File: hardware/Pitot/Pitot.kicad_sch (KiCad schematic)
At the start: 35 parts, among them J1 53307-2471, J2 Conn_01x05, J3 MX150_02x06_Vertical, U2 LDO40LPURY

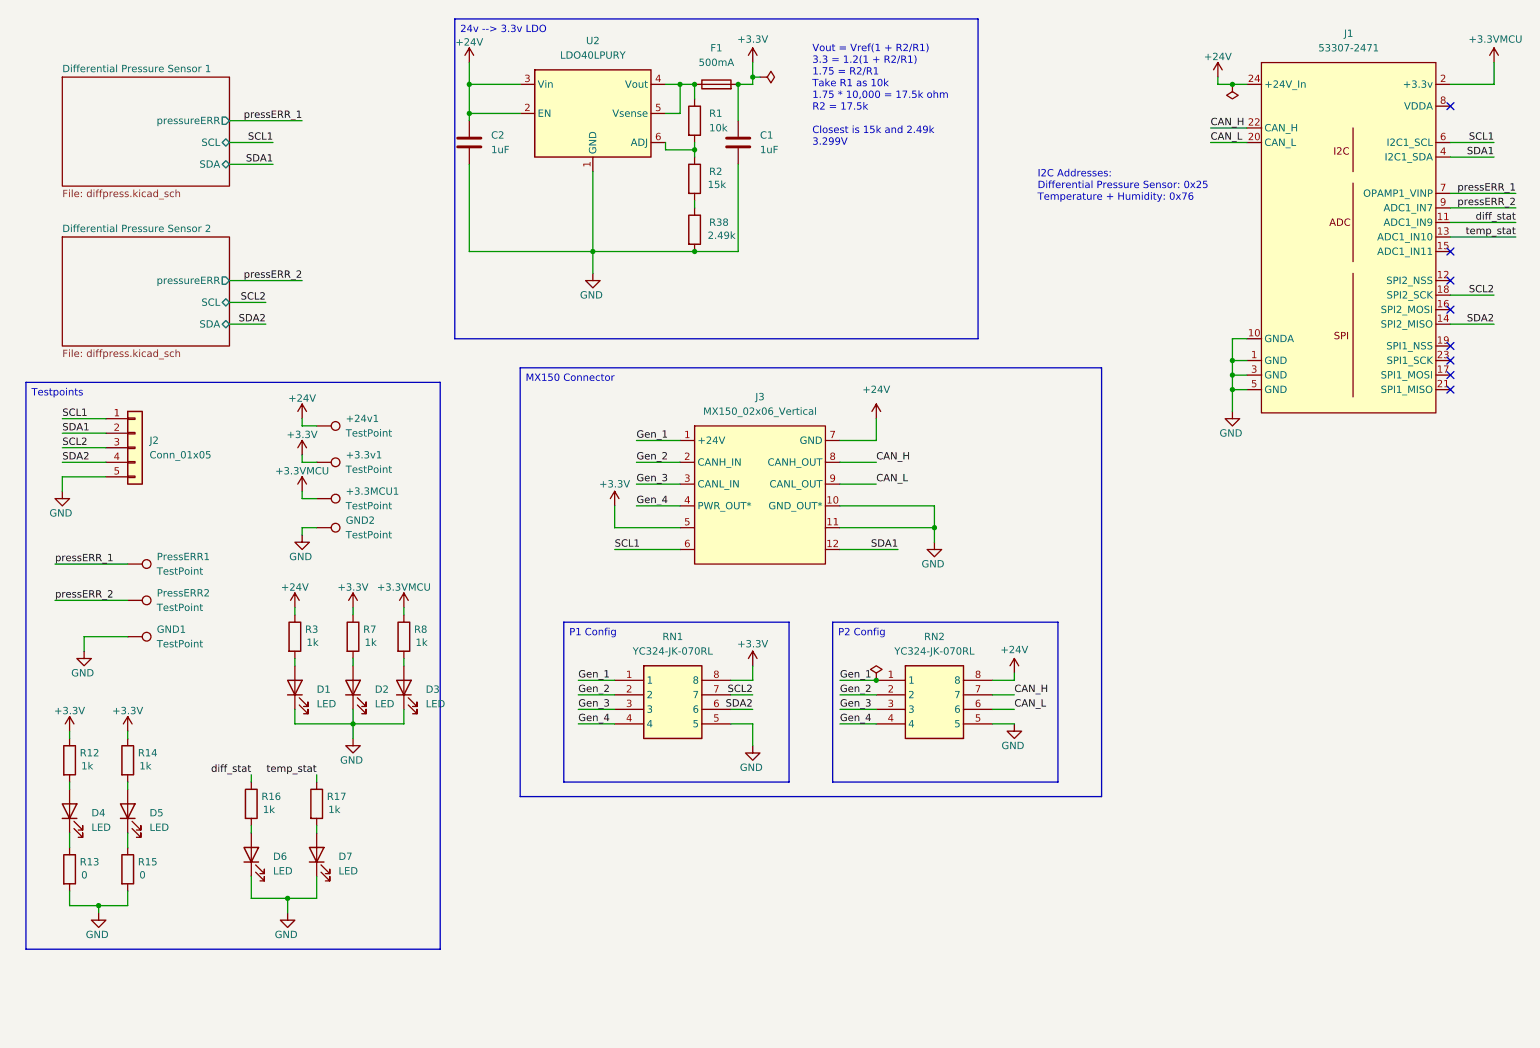
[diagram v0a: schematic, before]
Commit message: small changes, cubemx needs checking
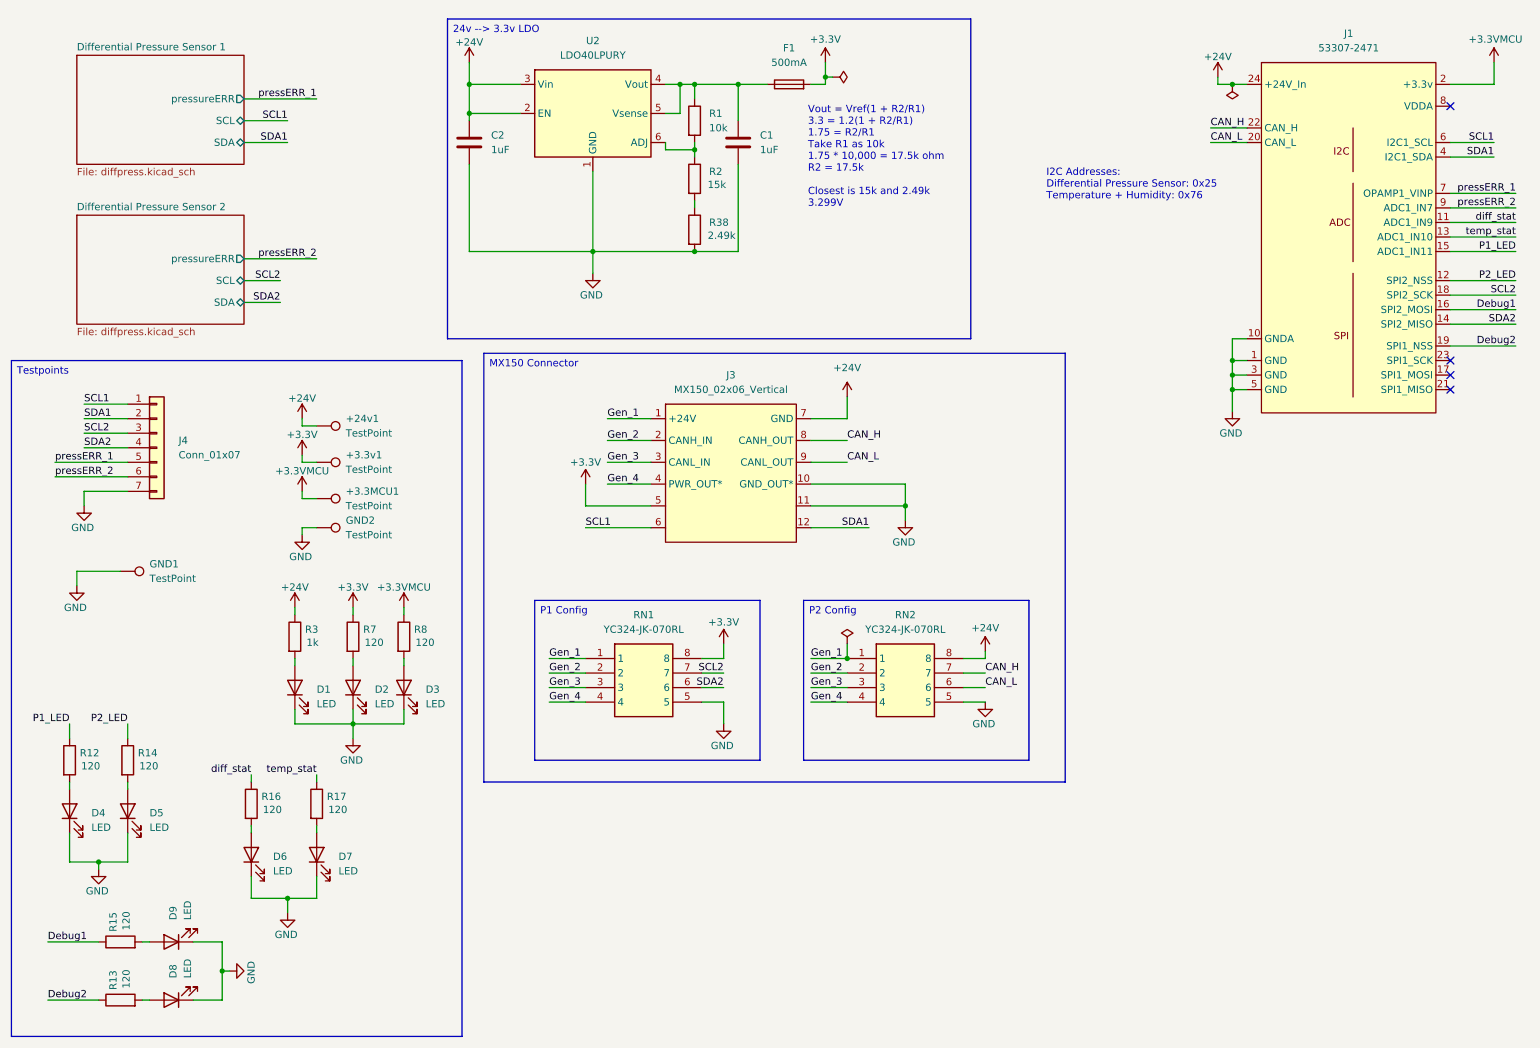
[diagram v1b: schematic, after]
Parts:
- removed J2: Conn_01x05, Connector_PinSocket_2.54mm:PinSocket_1x05_P2.54mm_Vertical, symbol Connector_Generic:Conn_01x05
- removed PressERR1, PressERR2: TestPoint, TestPoint:TestPoint_Pad_1.0x1.0mm, symbol Connector:TestPoint
- added D8, D9: LED, LED_SMD:LED_0603_1608Metric_Pad1.05x0.95mm_HandSolder, symbol Device:LED
- added J4: Conn_01x07, symbol Connector_Generic:Conn_01x07
- R12, R14, R16, R17, R7, R8: value 1k -> 120
- R13, R15: value 0 -> 120; P/N CRCW06030000Z0EE -> CRCW06031K00FKEI
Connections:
- net +3.3V: no longer C1.1, R12.1, R14.1
- net GND: now also D4.1 (K), D5.1 (K), D8.1 (K), D9.1 (K), J4.7 (Pin_7); no longer R13.2, R15.2
- net SCL1: now also J4.1 (Pin_1)
- net SCL2: now also J4.3 (Pin_3)
- net SDA1: now also J4.2 (Pin_2)
- net SDA2: now also J4.4 (Pin_4)
- net pressERR_1: now also J4.5 (Pin_5)
- net pressERR_2: now also J4.6 (Pin_6)
- net Debug2: now reaches R13.1
- net Debug2: now also J1.19 (SPI1_NSS); no longer D4.1 (K)
- net at F1.1, R1.1, U2.4 (Vout)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: now also C1.1
- net P2_LED: now reaches J1.12 (SPI2_NSS)
- net P2_LED: now also R14.1
- net P1_LED: now reaches J1.15 (ADC1_IN11)
- net P1_LED: now also R12.1
- net Debug1: now reaches J1.16 (SPI2_MOSI)
- net Debug1: now also R15.1
- new net: D9.2 (A), R15.2
- new net: D8.2 (A), R13.2
- no-connect marks 8 -> 4
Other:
- moved on the sheet: F1, GND1, J3, RN1, RN2

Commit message: finished layout
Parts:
- J4: footprint (none) -> Connector_PinHeader_2.54mm:PinHeader_2x04_P2.54mm_Vertical
- R3: value 1k -> 4.7k
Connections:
- net +24V: now also RN2.5; no longer RN2.8
- net GND: now also RN2.8; no longer RN2.5
- net Gen_1: now also RN2.4; no longer RN2.1
- net Gen_2: now also RN1.3; no longer RN1.2
- net Gen_3: now also RN1.2; no longer RN1.3
- net Gen_4: now also RN2.1; no longer RN2.4
- net SCL2: now also RN1.6; no longer RN1.7
- net SDA2: now also RN1.7; no longer RN1.6
- net CAN_H renamed CAN_+
- net CAN_L renamed CAN_-
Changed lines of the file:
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@@
 		)
 	)
-	(text_box "Testpoints\n"
-		(exclude_from_sim no)
-		(at 15.24 74.93 0)
-		(size 78.74 118.11)
-		(margins 0.9525 0.9525 0.9525 0.9525)
-		(stroke
-			(width 0)
-			(type solid)
-		)
-		(fill
-			(type none)
-		)
-		(effects
-			(font
-				(size 1.27 1.27)
-			)
-			(justify left top)
-		)
-	)
 	(text_box "24v --> 3.3v LDO\n"
 		(exclude_from_sim no)
@@
 	(wire
 		(pts
-			(xy 185.42 125.73) (xy 185.42 127)
-		)
-		(stroke
-			(width 0)
-			(type default)
-		)
-	)
-	(wire
-		(pts
 			(xy 171.45 100.33) (xy 171.45 102.87)
 		)
@@
 	(wire
 		(pts
+			(xy 191.77 123.19) (xy 191.77 134.62)
+		)
+		(stroke
+			(width 0)
+			(type default)
+		)
+	)
+	(wire
+		(pts
 			(xy 34.29 111.76) (xy 26.67 111.76)
 		)
@@
 	(wire
 		(pts
+			(xy 185.42 119.38) (xy 181.61 119.38)
+		)
+		(stroke
+			(width 0)
+			(type default)
+		)
+	)
+	(wire
+		(pts
+			(xy 181.61 132.08) (xy 185.42 132.08)
+		)
+		(stroke
+			(width 0)
+			(type default)
+		)
+	)
+	(wire
+		(pts
 			(xy 25.4 148.59) (xy 25.4 149.86)
 		)
@@
 	(wire
 		(pts
-			(xy 181.61 127) (xy 185.42 127)
-		)
-		(stroke
-			(width 0)
-			(type default)
-		)
-	)
-	(wire
-		(pts
 			(xy 52.07 186.69) (xy 52.07 181.61)
 		)
@@
 	(wire
 		(pts
-			(xy 185.42 134.62) (xy 181.61 134.62)
-		)
-		(stroke
-			(width 0)
-			(type default)
-		)
-	)
-	(wire
-		(pts
 			(xy 119.38 85.09) (xy 127 85.09)
 		)
@@
 	(wire
 		(pts
+			(xy 181.61 129.54) (xy 185.42 129.54)
+		)
+		(stroke
+			(width 0)
+			(type default)
+		)
+	)
+	(wire
+		(pts
 			(xy 135.89 134.62) (xy 139.7 134.62)
 		)
@@
 	(wire
 		(pts
-			(xy 181.61 132.08) (xy 185.42 132.08)
+			(xy 266.7 53.34) (xy 278.13 53.34)
 		)
 		(stroke
@@
 	(wire
 		(pts
-			(xy 266.7 53.34) (xy 278.13 53.34)
+			(xy 129.54 31.75) (xy 132.08 31.75)
 		)
 		(stroke
@@
 	(wire
 		(pts
-			(xy 129.54 31.75) (xy 132.08 31.75)
+			(xy 64.77 138.43) (xy 74.93 138.43)
 		)
 		(stroke
@@
 	(wire
 		(pts
-			(xy 64.77 138.43) (xy 74.93 138.43)
+			(xy 181.61 119.38) (xy 181.61 127)
 		)
 		(stroke
@@
 	(wire
 		(pts
-			(xy 38.1 186.69) (xy 39.37 186.69)
+			(xy 181.61 134.62) (xy 191.77 134.62)
 		)
 		(stroke
@@
 	(wire
 		(pts
-			(xy 139.7 124.46) (xy 139.7 127)
+			(xy 38.1 186.69) (xy 39.37 186.69)
 		)
 		(stroke
@@
 	(wire
 		(pts
-			(xy 25.4 157.48) (xy 25.4 162.56)
+			(xy 139.7 124.46) (xy 139.7 127)
 		)
 		(stroke
@@
 	(wire
 		(pts
-			(xy 181.61 129.54) (xy 185.42 129.54)
+			(xy 25.4 157.48) (xy 25.4 162.56)
 		)
 		(stroke
@@
 		)
 	)
-	(label "SDA2"
+	(label "SCL2"
 		(at 139.7 132.08 180)
 		(effects
@@
 		)
 	)
-	(label "CAN_L"
+	(label "CAN_-"
 		(at 161.29 92.71 0)
 		(effects
@@
 		)
 	)
-	(label "Gen_3"
+	(label "Gen_2"
 		(at 109.22 132.08 0)
 		(effects
@@
 		)
 	)
-	(label "CAN_L"
+	(label "CAN_-"
 		(at 224.79 36.83 0)
 		(effects
@@
 		)
 	)
-	(label "Gen_2"
+	(label "Gen_3"
 		(at 109.22 129.54 0)
 		(effects
@@
 		)
 	)
-	(label "CAN_L"
-		(at 185.42 132.08 0)
+	(label "P1_LED"
+		(at 278.13 55.88 180)
 		(effects
 			(font
 				(size 1.27 1.27)
 			)
-			(justify left bottom)
+			(justify right bottom)
 		)
 	)
-	(label "P1_LED"
-		(at 278.13 55.88 180)
+	(label "CAN_-"
+		(at 185.42 132.08 0)
 		(effects
 			(font
 				(size 1.27 1.27)
 			)
-			(justify right bottom)
+			(justify left bottom)
 		)
 	)
-	(label "Gen_4"
+	(label "Gen_1"
 		(at 154.94 134.62 0)
 		(effects
@@
 		)
 	)
-	(label "Gen_1"
+	(label "Gen_4"
 		(at 154.94 127 0)
 		(effects
@@
 		)
 	)
+	(label "CAN_+"
+		(at 185.42 129.54 0)
+		(effects
+			(font
+				(size 1.27 1.27)
+			)
+			(justify left bottom)
+		)
+	)
 	(label "temp_stat"
 		(at 68.58 147.32 180)
@@
 		)
 	)
-	(label "CAN_H"
+	(label "CAN_+"
 		(at 161.29 88.9 0)
 		(effects
@@
 		)
 	)
-	(label "SCL2"
+	(label "SDA2"
 		(at 139.7 129.54 180)
 		(effects
@@
 		)
 	)
-	(label "CAN_H"
+	(label "CAN_+"
 		(at 224.79 34.29 0)
 		(effects
@@
 		)
 	)
-	(label "CAN_H"
-		(at 185.42 129.54 0)
-		(effects
-			(font
-				(size 1.27 1.27)
-			)
-			(justify left bottom)
-		)
-	)
 	(label "pressERR_1"
 		(at 22.86 92.71 0)
@@
 			)
 		)
-		(property "Footprint" ""
+		(property "Footprint" "Connector_PinHeader_2.54mm:PinHeader_2x04_P2.54mm_Vertical"
 			(at 40.64 90.17 0)
 			(effects
@@
 			)
 		)
-		(property "Value" "1k"
+		(property "Value" "4.7k"
 			(at 66.802 124.2061 0)
 			(effects
@@
 	(symbol
 		(lib_id "power:GND")
-		(at 185.42 134.62 0)
+		(at 185.42 119.38 0)
 		(unit 1)
 		(exclude_from_sim no)
@@
 		(on_board yes)
 		(dnp no)
-		(property "Reference" "#PWR029"
-			(at 185.42 140.97 0)
+		(property "Reference" "#PWR035"
+			(at 185.42 125.73 0)
 			(effects
 				(font
@@
 		)
 		(property "Value" "GND"
-			(at 185.166 138.43 0)
+			(at 185.166 123.19 0)
 			(effects
 				(font
@@
 		)
 		(property "Footprint" ""
-			(at 185.42 134.62 0)
+			(at 185.42 119.38 0)
 			(effects
 				(font
@@
 		)
 		(property "Datasheet" ""
-			(at 185.42 134.62 0)
+			(at 185.42 119.38 0)
 			(effects
 				(font
@@
 		)
 		(property "Description" "Power symbol creates a global label with name \"GND\" , ground"
-			(at 185.42 134.62 0)
+			(at 185.42 119.38 0)
 			(effects
 				(font
@@
 			(project "Pitot"
 				(path "/b92f2323-f48d-45bc-8bf4-2cff87ecc0bc"
-					(reference "#PWR029")
+					(reference "#PWR035")
 					(unit 1)
 				)
@@
 	(symbol
 		(lib_id "power:+24V")
-		(at 185.42 125.73 0)
+		(at 191.77 123.19 0)
 		(unit 1)
 		(exclude_from_sim no)
@@
 		(dnp no)
 		(property "Reference" "#PWR028"
-			(at 185.42 129.54 0)
+			(at 191.77 127 0)
 			(effects
 				(font
@@
 		)
 		(property "Value" "+24V"
-			(at 185.42 121.666 0)
+			(at 191.77 119.126 0)
 			(effects
 				(font
@@
 		)
 		(property "Footprint" ""
-			(at 185.42 125.73 0)
+			(at 191.77 123.19 0)
 			(effects
 				(font
@@
 		)
 		(property "Datasheet" ""
-			(at 185.42 125.73 0)
+			(at 191.77 123.19 0)
 			(effects
 				(font
@@
 		)
 		(property "Description" "Power symbol creates a global label with name \"+24V\""
-			(at 185.42 125.73 0)
+			(at 191.77 123.19 0)
 			(effects
 				(font

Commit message: fixed routing for air-sus, should be much better now. added silkscreen
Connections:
- net Debug1: now also J1.13 (ADC1_IN10); no longer J1.16 (SPI2_MOSI)
- net Debug2: now also J1.11 (ADC1_IN9); no longer J1.19 (SPI1_NSS)
- net P2_LED: now also J1.17 (SPI1_MOSI); no longer J1.12 (SPI2_NSS)
- net diff_stat: now also J1.7 (OPAMP1_VINP); no longer J1.11 (ADC1_IN9)
- net pressERR_1: now also J1.12 (SPI2_NSS); no longer J1.7 (OPAMP1_VINP)
- net pressERR_2: now also J1.16 (SPI2_MOSI); no longer J1.9 (ADC1_IN7)
- net temp_stat: now also J1.9 (ADC1_IN7); no longer J1.13 (ADC1_IN10)
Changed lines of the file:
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@@
 	)
 	(no_connect
-		(at 266.7 77.47)
+		(at 266.7 30.48)
 	)
 	(no_connect
-		(at 266.7 30.48)
+		(at 266.7 74.93)
 	)
 	(no_connect
-		(at 266.7 80.01)
+		(at 266.7 72.39)
 	)
 	(no_connect
-		(at 266.7 74.93)
+		(at 266.7 80.01)
 	)
 	(wire
@@
 	(wire
 		(pts
-			(xy 266.7 72.39) (xy 278.13 72.39)
-		)
-		(stroke
-			(width 0)
-			(type default)
-		)
-	)
-	(wire
-		(pts
 			(xy 115.57 104.14) (xy 127 104.14)
 		)
@@
 	(wire
 		(pts
-			(xy 266.7 60.96) (xy 278.13 60.96)
+			(xy 119.38 92.71) (xy 127 92.71)
 		)
 		(stroke
@@
 	(wire
 		(pts
-			(xy 119.38 92.71) (xy 127 92.71)
+			(xy 30.48 162.56) (xy 35.56 162.56)
 		)
 		(stroke
@@
 	(wire
 		(pts
-			(xy 30.48 162.56) (xy 35.56 162.56)
+			(xy 266.7 48.26) (xy 278.13 48.26)
 		)
 		(stroke
@@
 	(wire
 		(pts
-			(xy 266.7 48.26) (xy 278.13 48.26)
+			(xy 266.7 66.04) (xy 278.13 66.04)
 		)
 		(stroke
@@
 	(wire
 		(pts
-			(xy 134.62 55.88) (xy 142.24 55.88)
+			(xy 266.7 60.96) (xy 278.13 60.96)
 		)
 		(stroke
@@
 	(wire
 		(pts
-			(xy 228.6 74.93) (xy 228.6 77.47)
+			(xy 134.62 55.88) (xy 142.24 55.88)
 		)
 		(stroke
@@
 	(wire
 		(pts
-			(xy 116.84 41.91) (xy 116.84 55.88)
+			(xy 228.6 74.93) (xy 228.6 77.47)
 		)
 		(stroke
@@
 	(wire
 		(pts
-			(xy 95.25 40.64) (xy 95.25 55.88)
+			(xy 116.84 41.91) (xy 116.84 55.88)
 		)
 		(stroke
@@
 	(wire
 		(pts
-			(xy 115.57 96.52) (xy 115.57 100.33)
+			(xy 95.25 40.64) (xy 95.25 55.88)
 		)
 		(stroke
@@
 	(wire
 		(pts
-			(xy 134.62 26.67) (xy 142.24 26.67)
+			(xy 115.57 96.52) (xy 115.57 100.33)
 		)
 		(stroke
@@
 	(wire
 		(pts
-			(xy 35.56 148.59) (xy 35.56 149.86)
+			(xy 134.62 26.67) (xy 142.24 26.67)
 		)
 		(stroke
@@
 	(wire
 		(pts
-			(xy 228.6 71.12) (xy 228.6 74.93)
+			(xy 35.56 148.59) (xy 35.56 149.86)
 		)
 		(stroke
@@
 	(wire
 		(pts
-			(xy 266.7 66.04) (xy 278.13 66.04)
+			(xy 228.6 71.12) (xy 228.6 74.93)
 		)
 		(stroke
@@
 	(wire
 		(pts
+			(xy 266.7 77.47) (xy 278.13 77.47)
+		)
+		(stroke
+			(width 0)
+			(type default)
+		)
+	)
+	(wire
+		(pts
 			(xy 83.82 138.43) (xy 83.82 135.89)
 		)
@@
 		)
 	)
-	(label "Debug2"
-		(at 278.13 72.39 180)
-		(effects
-			(font
-				(size 1.27 1.27)
-			)
-			(justify right bottom)
-		)
-	)
 	(label "SCL1"
 		(at 115.57 104.14 0)
@@
 	)
 	(label "pressERR_2"
+		(at 278.13 66.04 180)
+		(effects
+			(font
+				(size 1.27 1.27)
+			)
+			(justify right bottom)
+		)
+	)
+	(label "temp_stat"
 		(at 278.13 48.26 180)
 		(effects
@@
 		)
 	)
-	(label "pressERR_1"
-		(at 278.13 45.72 180)
-		(effects
-			(font
-				(size 1.27 1.27)
-			)
-			(justify right bottom)
-		)
-	)
 	(label "SCL2"
 		(at 62.23 60.96 180)
@@
 	)
 	(label "Debug1"
-		(at 278.13 66.04 180)
-		(effects
-			(font
-				(size 1.27 1.27)
-			)
-			(justify right bottom)
-		)
-	)
-	(label "Debug1"
 		(at 21.59 176.53 0)
 		(effects
@@
 		)
 	)
-	(label "pressERR_1"
-		(at 68.58 29.21 180)
+	(label "diff_stat"
+		(at 278.13 45.72 180)
 		(effects
 			(font
@@
 		)
 	)
-	(label "SCL2"
-		(at 27.94 87.63 0)
+	(label "pressERR_1"
+		(at 68.58 29.21 180)
 		(effects
 			(font
 				(size 1.27 1.27)
 			)
-			(justify left bottom)
+			(justify right bottom)
 		)
 	)
-	(label "P1_LED"
-		(at 278.13 55.88 180)
+	(label "SCL2"
+		(at 27.94 87.63 0)
 		(effects
 			(font
 				(size 1.27 1.27)
 			)
-			(justify right bottom)
+			(justify left bottom)
 		)
 	)
@@
 	)
 	(label "Debug2"
+		(at 278.13 50.8 180)
+		(effects
+			(font
+				(size 1.27 1.27)
+			)
+			(justify right bottom)
+		)
+	)
+	(label "Debug2"
 		(at 21.59 186.69 0)
 		(effects
@@
 		)
 	)
-	(label "P2_LED"
+	(label "pressERR_1"
 		(at 278.13 60.96 180)
 		(effects
@@
 		)
 	)
-	(label "diff_stat"
-		(at 278.13 50.8 180)
+	(label "Debug1"
+		(at 278.13 53.34 180)
 		(effects
 			(font
@@
 		)
 	)
-	(label "temp_stat"
-		(at 278.13 53.34 180)
+	(label "P1_LED"
+		(at 278.13 55.88 180)
 		(effects
 			(font
@@
 		)
 	)
+	(label "P2_LED"
+		(at 278.13 77.47 180)
+		(effects
+			(font
+				(size 1.27 1.27)
+			)
+			(justify right bottom)
+		)
+	)
